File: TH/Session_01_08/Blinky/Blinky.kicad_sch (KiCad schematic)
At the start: 12 parts

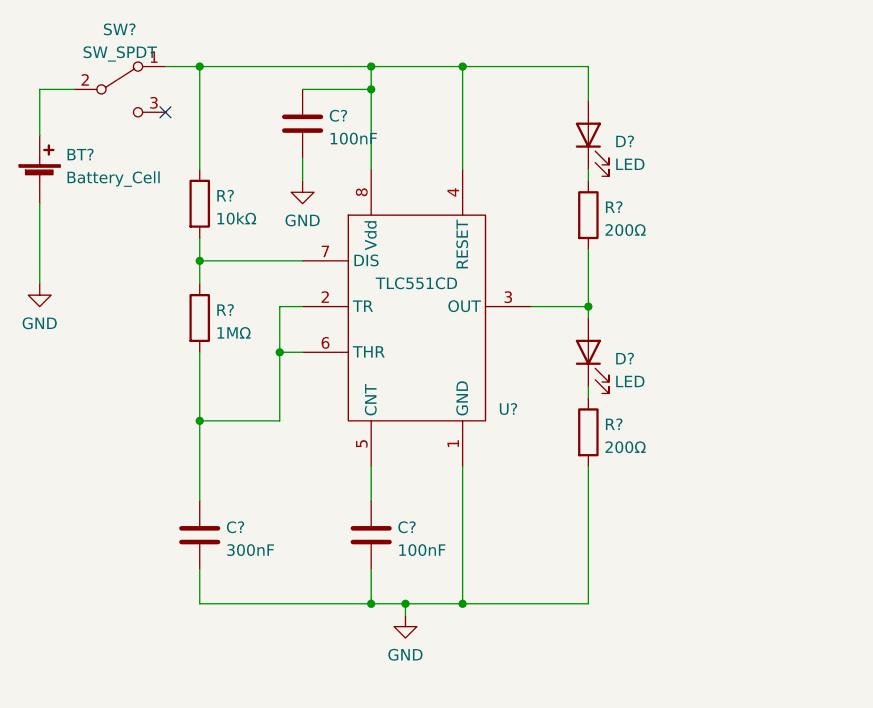
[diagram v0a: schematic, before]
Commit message: Revamps the through-hole project as transistor based
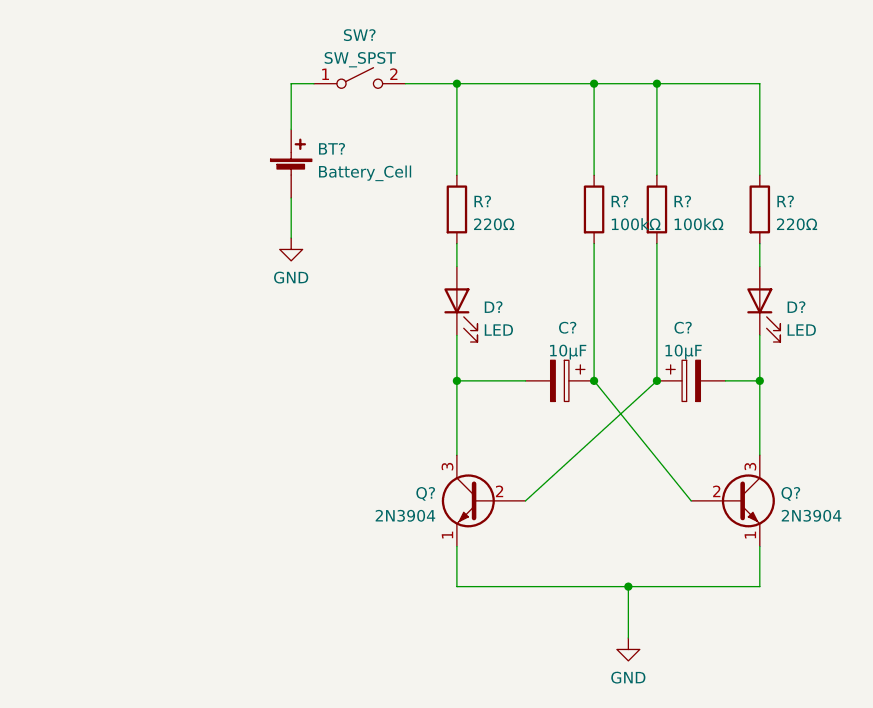
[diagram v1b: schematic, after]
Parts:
- removed BT?: Battery_Cell, Battery:BatteryHolder_Keystone_3000_1x12mm, symbol Device:Battery_Cell
- removed C? (x2): 100nF, Capacitor_THT:C_Disc_D5.0mm_W2.5mm_P5.00mm, symbol Device:C
- removed C?: 300nF, Capacitor_THT:C_Disc_D5.0mm_W2.5mm_P5.00mm, symbol Device:C
- removed D? (x2): LED, LED_THT:LED_D5.0mm, symbol Device:LED
- removed R? (x2): 200Ω, Resistor_THT:R_Axial_DIN0207_L6.3mm_D2.5mm_P10.16mm_Horizontal, symbol Device:R
- removed R?: 10kΩ, Resistor_THT:R_Axial_DIN0207_L6.3mm_D2.5mm_P10.16mm_Horizontal, symbol Device:R
- removed R?: 1MΩ, Resistor_THT:R_Axial_DIN0207_L6.3mm_D2.5mm_P10.16mm_Horizontal, symbol Device:R
- removed SW?: SW_SPDT, Resistor_THT:R_Axial_DIN0207_L6.3mm_D2.5mm_P10.16mm_Horizontal, symbol Switch:SW_SPDT
- removed U?: TLC551CD‎, Package_DIP:DIP-8_W7.62mm_Socket, symbol Blinky:TLC551CD‎
- added BT?: Battery_Cell, Battery:BatteryHolder_Keystone_3000_1x12mm, symbol Device:Battery_Cell
- added C? (x2): 10μF, Capacitor_THT:CP_Radial_D5.0mm_P2.50mm, symbol Device:C_Polarized
- added D? (x2): LED, LED_THT:LED_D5.0mm, symbol Device:LED
- added Q? (x2): 2N3904, Package_TO_SOT_THT:TO-92_Inline, symbol Transistor_BJT:2N3904
- added R? (x2): 100kΩ, Resistor_THT:R_Axial_DIN0207_L6.3mm_D2.5mm_P2.54mm_Vertical, symbol Device:R
- added R? (x2): 220Ω, Resistor_THT:R_Axial_DIN0207_L6.3mm_D2.5mm_P2.54mm_Vertical, symbol Device:R
- added SW?: SW_SPST, Blinky_ZAM:SSK-1202, symbol Switch:SW_SPST
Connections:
- net GND: now also BT?.2 (-), Q?.1 (E), Q?.1 (E)
- new net: R?.1, R?.1, R?.1, R?.1, SW?.2 (B)
- new net: C?.1, Q?.2 (B), R?.2 (x2)
- new net: C?.2, D?.1 (K), Q?.3 (C) (x2)
- new net: D?.2 (A), R?.2 (x2)
- new net: BT?.1 (+), SW?.1 (A)
- no-connect marks 1 -> 0

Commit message: Makes corrections to the design rules
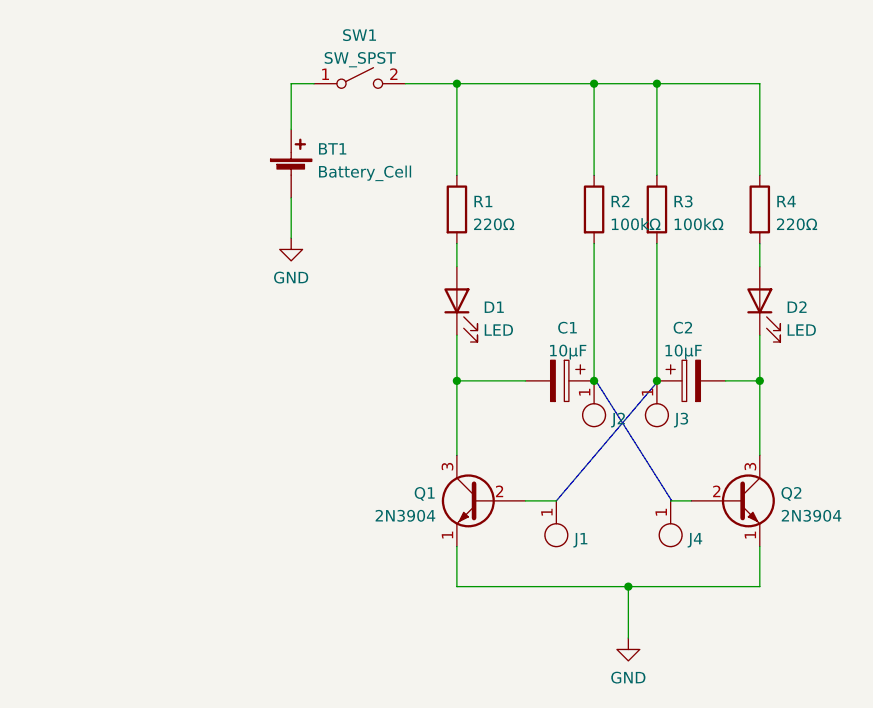
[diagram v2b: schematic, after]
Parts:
- added J1, J2, J3, J4: Jumper_1, TestPoint:TestPoint_THTPad_2.0x2.0mm_Drill1.0mm, symbol Blinky:Jumper_1
- gave numbers to parts that had none: 12
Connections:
- net at C1.1, R2.2: now also J2.1; no longer Q2.2 (B)
- net at C2.1, R3.2: now also J3.1; no longer Q1.2 (B)
- new net: J4.1, Q2.2 (B)
- new net: J1.1, Q1.2 (B)
